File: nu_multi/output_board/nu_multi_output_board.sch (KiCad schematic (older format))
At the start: 2 parts, among them J1 CONN_02X07, J2 CONN_02X05

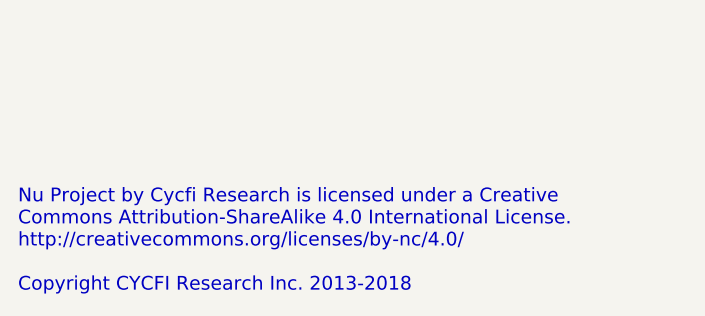
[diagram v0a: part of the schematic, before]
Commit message: Updates; added nu multi-8 mounting board
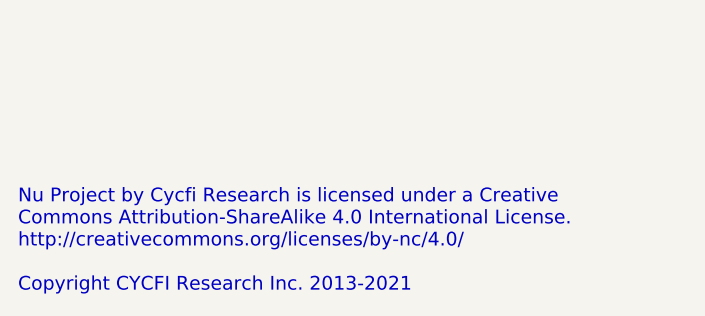
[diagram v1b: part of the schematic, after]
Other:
- note added: "Nu Project by Cycfi Research is licensed under a Creative \nCommons Attribution-ShareAlike 4.0 International License. \nhttp://creativecommons.org/licenses/by-nc/4.0/\n\nCopyright CYCFI Research Inc. 2013-2021"
- note removed: "Nu Project by Cycfi Research is licensed under a Creative \nCommons Attribution-ShareAlike 4.0 International License. \nhttp://creativecommons.org/licenses/by-nc/4.0/\n\nCopyright CYCFI Research Inc. 2013-2018"
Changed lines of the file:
@@
 Title "Output Board"
 Date "2018-04-17"
-Rev ""
-Comp "Document Number: 2018008"
+Rev "2.5"
+Comp "Document Number: 2021012"
 Comment1 ""
 Comment2 ""
@@
 2x7 Female Pin Header 1mm Pitch
 Text Notes 2035 6835 0    60   ~ 0
-Nu Project by Cycfi Research is licensed under a Creative \nCommons Attribution-ShareAlike 4.0 International License. \nhttp://creativecommons.org/licenses/by-nc/4.0/\n\nCopyright CYCFI Research Inc. 2013-2018
+Nu Project by Cycfi Research is licensed under a Creative \nCommons Attribution-ShareAlike 4.0 International License. \nhttp://creativecommons.org/licenses/by-nc/4.0/\n\nCopyright CYCFI Research Inc. 2013-2021
 $Comp
 L nu_multi_output_board:CONN_02X05-conn J2
